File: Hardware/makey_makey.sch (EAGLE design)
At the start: 73 parts, among them U1 ATMEGA32U4TQFP, X1 USBSMD, Y1 16MHz

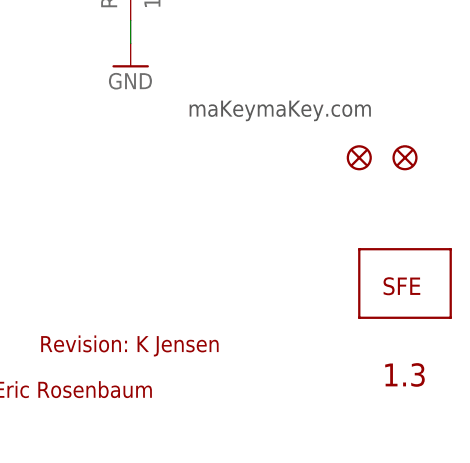
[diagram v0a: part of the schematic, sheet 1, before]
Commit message: Updated board layout.
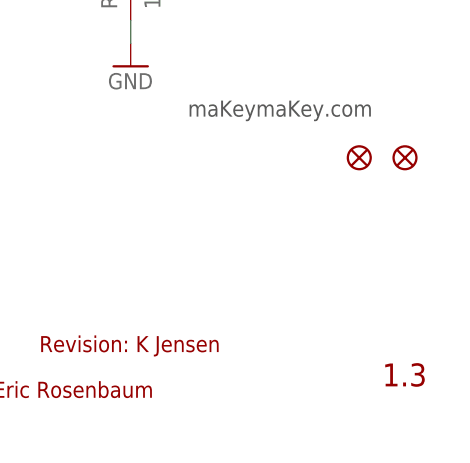
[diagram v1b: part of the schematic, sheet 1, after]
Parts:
- removed JP9: LOGO-SFENEW, SparkFun:LOGO-SFENEW
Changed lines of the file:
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@@
 <?xml version="1.0" encoding="utf-8"?>
 <!DOCTYPE eagle SYSTEM "eagle.dtd">
-<eagle version="6.4">
+<eagle version="7.2.0">
 <drawing>
 <settings>
@@
 <grid distance="0.1" unitdist="inch" unit="inch" style="lines" multiple="1" display="no" altdistance="0.01" altunitdist="inch" altunit="inch"/>
 <layers>
-<layer number="1" name="Top" color="4" fill="1" visible="yes" active="no"/>
-<layer number="2" name="Route2" color="1" fill="3" visible="yes" active="no"/>
-<layer number="3" name="Route3" color="4" fill="3" visible="yes" active="no"/>
-<layer number="4" name="Route4" color="1" fill="4" visible="yes" active="no"/>
-<layer number="5" name="Route5" color="4" fill="4" visible="yes" active="no"/>
-<layer number="6" name="Route6" color="1" fill="8" visible="yes" active="no"/>
-<layer number="7" name="Route7" color="4" fill="8" visible="yes" active="no"/>
-<layer number="8" name="Route8" color="1" fill="2" visible="yes" active="no"/>
-<layer number="9" name="Route9" color="4" fill="2" visible="yes" active="no"/>
-<layer number="10" name="Route10" color="1" fill="7" visible="yes" active="no"/>
-<layer number="11" name="Route11" color="4" fill="7" visible="yes" active="no"/>
-<layer number="12" name="Route12" color="1" fill="5" visible="yes" active="no"/>
-<layer number="13" name="Route13" color="4" fill="5" visible="yes" active="no"/>
-<layer number="14" name="Route14" color="1" fill="6" visible="yes" active="no"/>
-<layer number="15" name="Route15" color="4" fill="6" visible="yes" active="no"/>
-<layer number="16" name="Bottom" color="1" fill="1" visible="yes" active="no"/>
-<layer number="17" name="Pads" color="2" fill="1" visible="yes" active="no"/>
-<layer number="18" name="Vias" color="2" fill="1" visible="yes" active="no"/>
-<layer number="19" name="Unrouted" color="13" fill="1" visible="yes" active="no"/>
-<layer number="20" name="Dimension" color="6" fill="1" visible="yes" active="no"/>
-<layer number="21" name="tPlace" color="16" fill="1" visible="yes" active="no"/>
-<layer number="22" name="bPlace" color="14" fill="1" visible="yes" active="no"/>
-<layer number="23" name="tOrigins" color="15" fill="1" visible="yes" active="no"/>
-<layer number="24" name="bOrigins" color="15" fill="1" visible="yes" active="no"/>
-<layer number="25" name="tNames" color="7" fill="1" visible="yes" active="no"/>
-<layer number="26" name="bNames" color="7" fill="1" visible="yes" active="no"/>
-<layer number="27" name="tValues" color="7" fill="1" visible="yes" active="no"/>
-<layer number="28" name="bValues" color="7" fill="1" visible="yes" active="no"/>
+<layer number="1" name="Top" color="4" fill="1" visible="no" active="no"/>
+<layer number="2" name="Route2" color="1" fill="3" visible="no" active="no"/>
+<layer number="3" name="Route3" color="4" fill="3" visible="no" active="no"/>
+<layer number="4" name="Route4" color="1" fill="4" visible="no" active="no"/>
+<layer number="5" name="Route5" color="4" fill="4" visible="no" active="no"/>
+<layer number="6" name="Route6" color="1" fill="8" visible="no" active="no"/>
+<layer number="7" name="Route7" color="4" fill="8" visible="no" active="no"/>
+<layer number="8" name="Route8" color="1" fill="2" visible="no" active="no"/>
+<layer number="9" name="Route9" color="4" fill="2" visible="no" active="no"/>
+<layer number="10" name="Route10" color="1" fill="7" visible="no" active="no"/>
+<layer number="11" name="Route11" color="4" fill="7" visible="no" active="no"/>
+<layer number="12" name="Route12" color="1" fill="5" visible="no" active="no"/>
+<layer number="13" name="Route13" color="4" fill="5" visible="no" active="no"/>
+<layer number="14" name="Route14" color="1" fill="6" visible="no" active="no"/>
+<layer number="15" name="Route15" color="4" fill="6" visible="no" active="no"/>
+<layer number="16" name="Bottom" color="1" fill="1" visible="no" active="no"/>
+<layer number="17" name="Pads" color="2" fill="1" visible="no" active="no"/>
+<layer number="18" name="Vias" color="2" fill="1" visible="no" active="no"/>
+<layer number="19" name="Unrouted" color="13" fill="1" visible="no" active="no"/>
+<layer number="20" name="Dimension" color="6" fill="1" visible="no" active="no"/>
+<layer number="21" name="tPlace" color="16" fill="1" visible="no" active="no"/>
+<layer number="22" name="bPlace" color="14" fill="1" visible="no" active="no"/>
+<layer number="23" name="tOrigins" color="15" fill="1" visible="no" active="no"/>
+<layer number="24" name="bOrigins" color="15" fill="1" visible="no" active="no"/>
+<layer number="25" name="tNames" color="7" fill="1" visible="no" active="no"/>
+<layer number="26" name="bNames" color="7" fill="1" visible="no" active="no"/>
+<layer number="27" name="tValues" color="7" fill="1" visible="no" active="no"/>
+<layer number="28" name="bValues" color="7" fill="1" visible="no" active="no"/>
 <layer number="29" name="tStop" color="13" fill="1" visible="no" active="no"/>
 <layer number="30" name="bStop" color="7" fill="6" visible="no" active="no"/>
@@
 <layer number="35" name="tGlue" color="7" fill="4" visible="no" active="no"/>
 <layer number="36" name="bGlue" color="7" fill="5" visible="no" active="no"/>
-<layer number="37" name="tTest" color="7" fill="1" visible="yes" active="no"/>
-<layer number="38" name="bTest" color="7" fill="1" visible="yes" active="no"/>
+<layer number="37" name="tTest" color="7" fill="1" visible="no" active="no"/>
+<layer number="38" name="bTest" color="7" fill="1" visible="no" active="no"/>
 <layer number="39" name="tKeepout" color="4" fill="11" visible="no" active="no"/>
 <layer number="40" name="bKeepout" color="1" fill="11" visible="no" active="no"/>
@@
 <layer number="44" name="Drills" color="7" fill="1" visible="no" active="no"/>
 <layer number="45" name="Holes" color="7" fill="1" visible="no" active="no"/>
-<layer number="46" name="Milling" color="3" fill="1" visible="yes" active="no"/>
-<layer number="47" name="Measures" color="7" fill="1" visible="yes" active="no"/>
-<layer number="48" name="Document" color="7" fill="1" visible="yes" active="no"/>
-<layer number="49" name="Reference" color="13" fill="1" visible="yes" active="no"/>
-<layer number="50" name="dxf" color="7" fill="1" visible="yes" active="no"/>
-<layer number="51" name="tDocu" color="6" fill="1" visible="yes" active="no"/>
-<layer number="52" name="bDocu" color="7" fill="1" visible="yes" active="no"/>
-<layer number="53" name="tGND_GNDA" color="7" fill="9" visible="yes" active="no"/>
-<layer number="54" name="bGND_GNDA" color="1" fill="9" visible="yes" active="no"/>
-<layer number="56" name="wert" color="7" fill="1" visible="yes" active="no"/>
+<layer number="46" name="Milling" color="3" fill="1" visible="no" active="no"/>
+<layer number="47" name="Measures" color="7" fill="1" visible="no" active="no"/>
+<layer number="48" name="Document" color="7" fill="1" visible="no" active="no"/>
+<layer number="49" name="Reference" color="13" fill="1" visible="no" active="no"/>
+<layer number="50" name="dxf" color="7" fill="1" visible="no" active="no"/>
+<layer number="51" name="tDocu" color="6" fill="1" visible="no" active="no"/>
+<layer number="52" name="bDocu" color="7" fill="1" visible="no" active="no"/>
+<layer number="53" name="tGND_GNDA" color="7" fill="9" visible="no" active="no"/>
+<layer number="54" name="bGND_GNDA" color="1" fill="9" visible="no" active="no"/>
+<layer number="56" name="wert" color="7" fill="1" visible="no" active="no"/>
 <layer number="91" name="Nets" color="2" fill="1" visible="yes" active="yes"/>
 <layer number="92" name="Busses" color="1" fill="1" visible="yes" active="yes"/>
@@
 <part name="P+6" library="SparkFun" deviceset="VCC" device=""/>
 <part name="P+7" library="SparkFun" deviceset="VCC" device=""/>
-<part name="JP9" library="SparkFun" deviceset="LOGO-SFE" device="NEW"/>
 <part name="C5" library="SparkFun" deviceset="CAP" device="0603-CAP" value="0.1uF"/>
 <part name="GND5" library="SparkFun" deviceset="GND" device=""/>
@@
 <instance part="P+6" gate="1" x="93.98" y="45.72" rot="MR0"/>
 <instance part="P+7" gate="1" x="88.9" y="45.72" rot="MR0"/>
-<instance part="JP9" gate="G$1" x="241.3" y="17.78"/>
 <instance part="C5" gate="G$1" x="170.18" y="66.04" smashed="yes" rot="R180">
 <attribute name="NAME" x="171.196" y="66.167" size="1.778" layer="95"/>
